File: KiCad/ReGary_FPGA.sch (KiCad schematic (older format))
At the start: 28 parts, among them J1 Conn_01x02, U1 GW1N-UV1P5LQ100, U2 LM1117-3.3, U3 TPS73643DBV

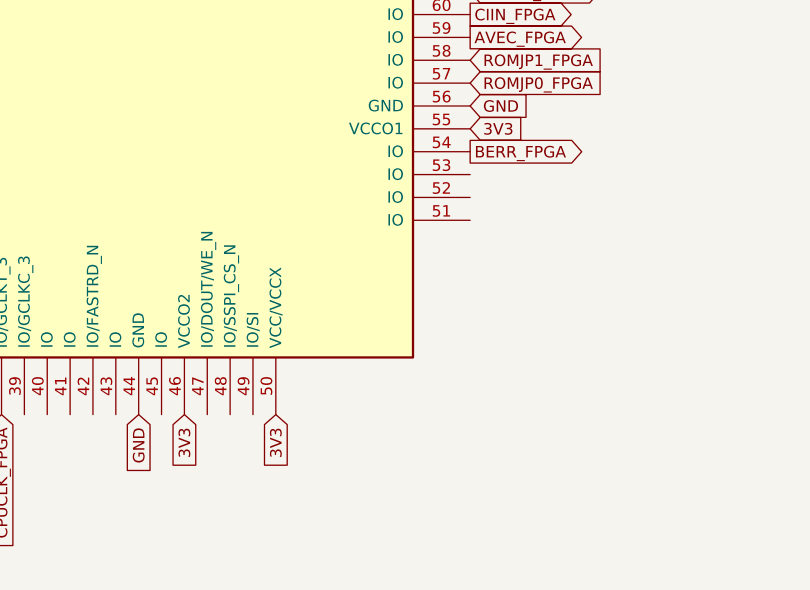
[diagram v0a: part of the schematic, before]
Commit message: More pin assignments and routing
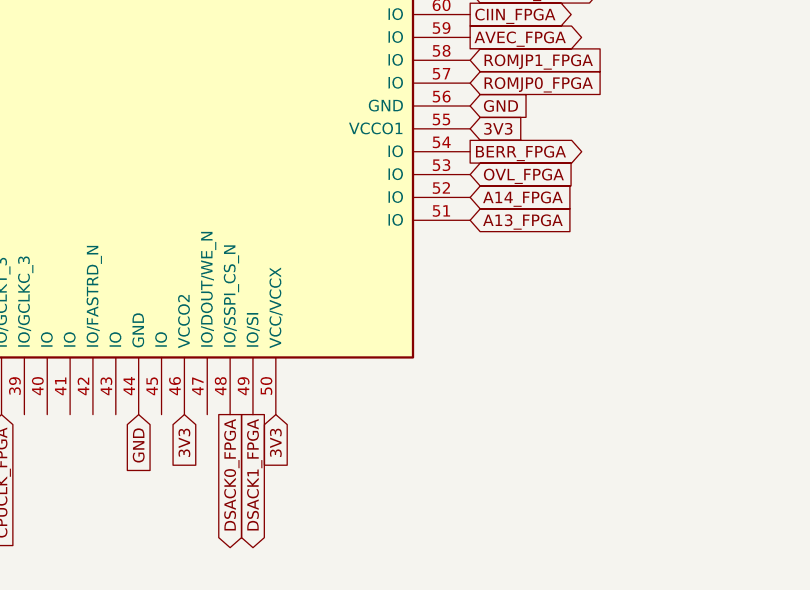
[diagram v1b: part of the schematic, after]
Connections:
- net labels added: A13_FPGA, A14_FPGA, DSACK0_FPGA, DSACK1_FPGA, OVL_FPGA
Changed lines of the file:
@@
 	8650 5150 9000 5150
 Connection ~ 8650 5150
+Text GLabel 5450 5250 2    50   Input ~ 0
+A14_FPGA
+Text GLabel 5450 5150 2    50   Input ~ 0
+OVL_FPGA
+Text GLabel 5450 5350 2    50   Input ~ 0
+A13_FPGA
+Text GLabel 4500 6200 3    50   Output ~ 0
+DSACK1_FPGA
+Text GLabel 4400 6200 3    50   Output ~ 0
+DSACK0_FPGA
 $EndSCHEMATC

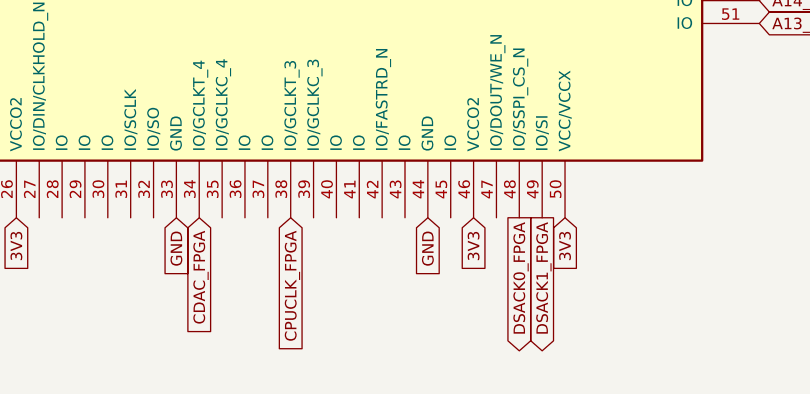
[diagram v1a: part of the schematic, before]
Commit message: More pin assignments and routing
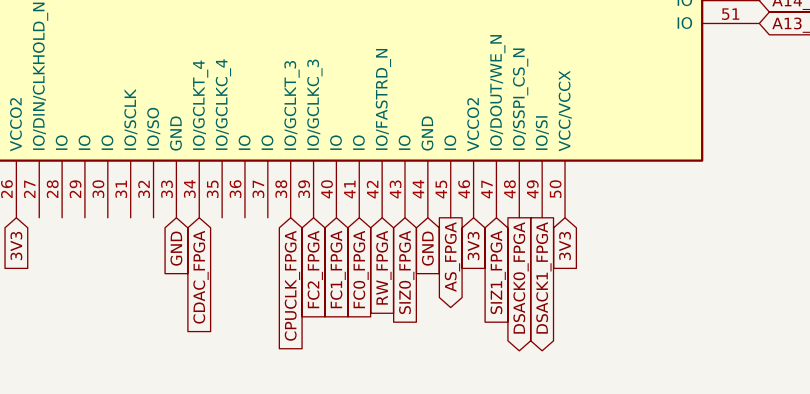
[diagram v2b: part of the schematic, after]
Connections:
- net labels added: AS_FPGA, FC0_FPGA, FC1_FPGA, FC2_FPGA, RW_FPGA, SIZ0_FPGA, SIZ1_FPGA
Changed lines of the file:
@@
 Text GLabel 4400 6200 3    50   Output ~ 0
 DSACK0_FPGA
+Text GLabel 4300 6200 3    50   Input ~ 0
+SIZ1_FPGA
+Text GLabel 3900 6200 3    50   Input ~ 0
+SIZ0_FPGA
+Text GLabel 3800 6200 3    50   Input ~ 0
+RW_FPGA
+Text GLabel 4100 6200 3    50   Output ~ 0
+AS_FPGA
+Text GLabel 3600 6200 3    50   Input ~ 0
+FC1_FPGA
+Text GLabel 3700 6200 3    50   Input ~ 0
+FC0_FPGA
+Text GLabel 3500 6200 3    50   Input ~ 0
+FC2_FPGA
 $EndSCHEMATC

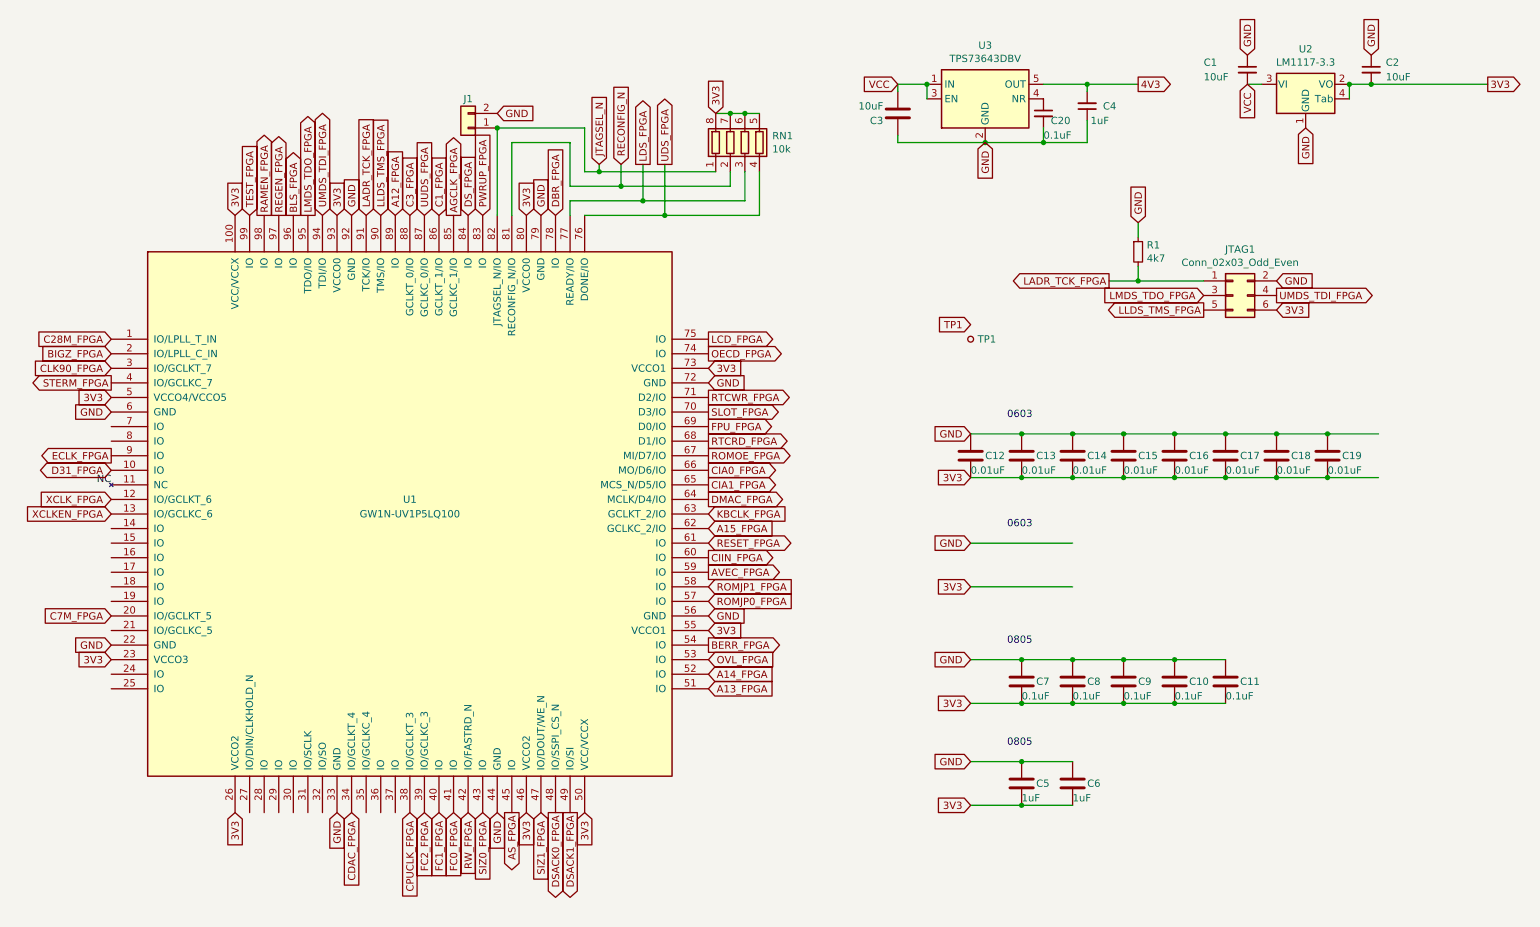
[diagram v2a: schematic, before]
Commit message: More signals to pin assignments and more routing done
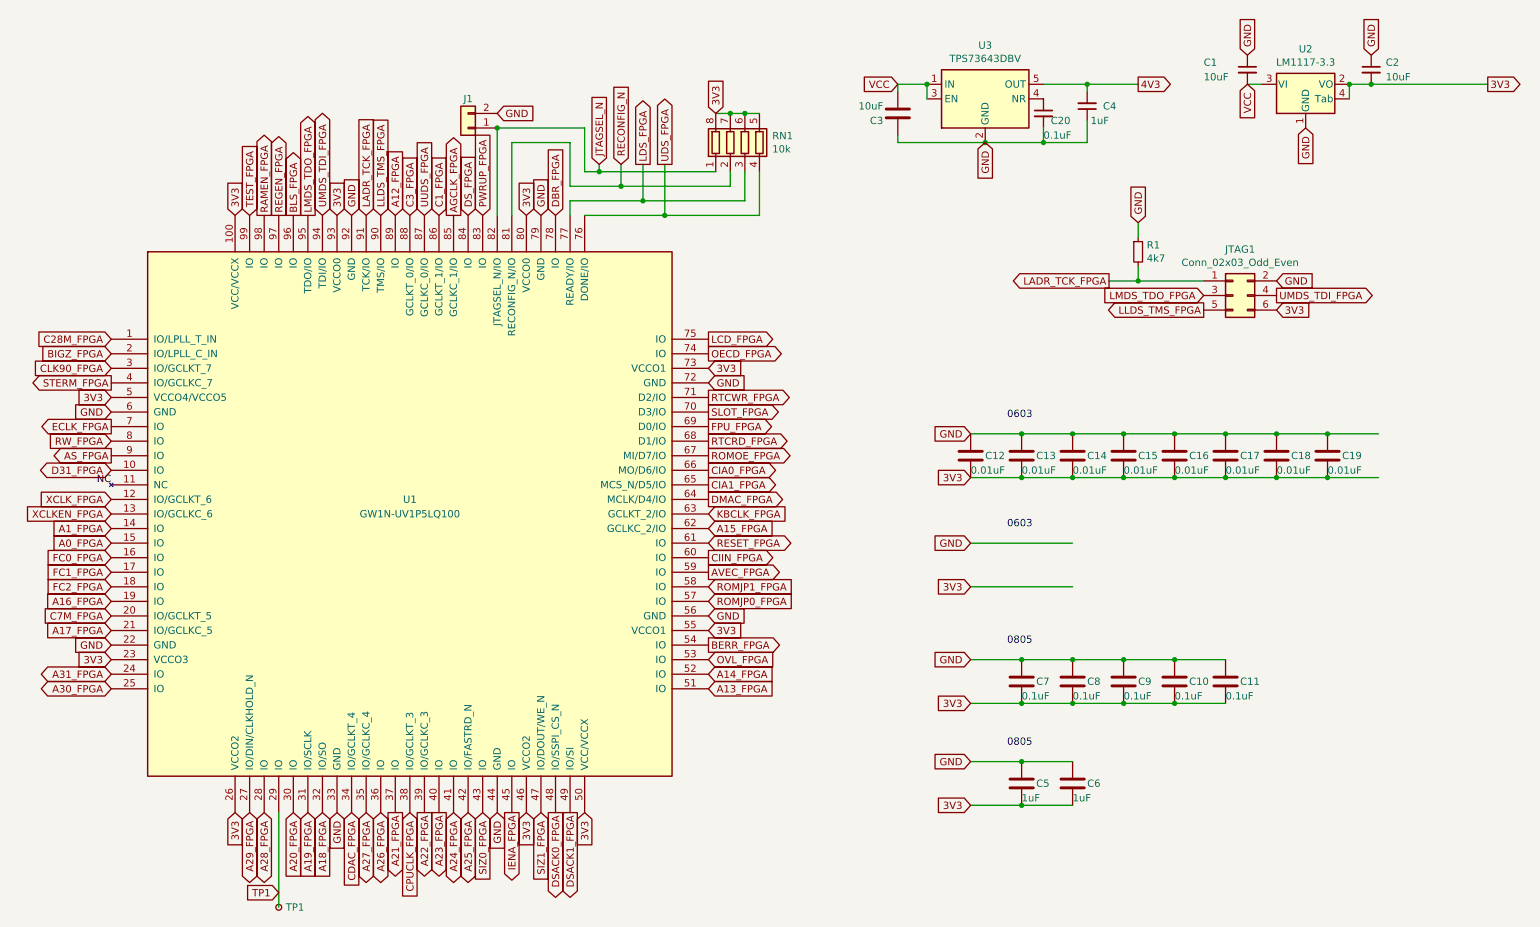
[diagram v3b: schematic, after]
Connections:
- net labels added: A0_FPGA, A16_FPGA, A17_FPGA, A18_FPGA, A19_FPGA, A1_FPGA, A20_FPGA, A21_FPGA, A22_FPGA, A23_FPGA, A24_FPGA, A25_FPGA, A26_FPGA, A27_FPGA, A28_FPGA, A29_FPGA, A30_FPGA, A31_FPGA, IENA_FPGA
- wire segments 77 -> 78
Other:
- moved on the sheet: TP1
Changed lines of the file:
@@
 	-1   0    0    1
 $EndComp
-Text GLabel 7250 2850 0    50   Input ~ 0
+Text GLabel 2500 6750 0    50   Input ~ 0
 TP1
 Wire Wire Line
@@
 L Connector:TestPoint_Small TP1
 U 1 1 655D4DC6
-P 7250 2950
-F 0 "TP1" H 7298 2950 50  0000 L CNN
-F 1 "TestPoint_Small" H 7298 2905 50  0001 L CNN
-F 2 "TestPoint:TestPoint_Pad_1.5x1.5mm" H 7450 2950 50  0001 C CNN
-F 3 "~" H 7450 2950 50  0001 C CNN
-	1    7250 2950
+P 2500 6850
+F 0 "TP1" H 2548 6850 50  0000 L CNN
+F 1 "TestPoint_Small" H 2548 6805 50  0001 L CNN
+F 2 "TestPoint:TestPoint_Pad_1.5x1.5mm" H 2700 6850 50  0001 C CNN
+F 3 "~" H 2700 6850 50  0001 C CNN
+	1    2500 6850
 	1    0    0    -1
 $EndComp
@@
 Text GLabel 3600 2100 1    50   Input ~ 0
 C1_FPGA
-Text GLabel 1350 3750 0    50   Output ~ 0
+Text GLabel 1350 3550 0    50   Output ~ 0
 ECLK_FPGA
 Text GLabel 2400 2100 1    50   Output ~ 0
@@
 Text GLabel 3900 6200 3    50   Input ~ 0
 SIZ0_FPGA
-Text GLabel 3800 6200 3    50   Input ~ 0
+Text GLabel 1350 3650 0    50   Input ~ 0
 RW_FPGA
+Text GLabel 1350 3750 0    50   Output ~ 0
+AS_FPGA
+Text GLabel 1350 4550 0    50   Input ~ 0
+FC1_FPGA
+Text GLabel 1350 4450 0    50   Input ~ 0
+FC0_FPGA
+Text GLabel 1350 4650 0    50   Input ~ 0
+FC2_FPGA
+Text GLabel 1350 4250 0    50   Input ~ 0
+A1_FPGA
+Text GLabel 1350 4350 0    50   Input ~ 0
+A0_FPGA
+Text GLabel 1350 5250 0    50   BiDi ~ 0
+A31_FPGA
+Text GLabel 1350 5350 0    50   BiDi ~ 0
+A30_FPGA
+Text GLabel 2300 6200 3    50   BiDi ~ 0
+A29_FPGA
+Text GLabel 2400 6200 3    50   BiDi ~ 0
+A28_FPGA
+Text GLabel 3100 6200 3    50   BiDi ~ 0
+A27_FPGA
+Text GLabel 3200 6200 3    50   BiDi ~ 0
+A26_FPGA
 Text GLabel 4100 6200 3    50   Output ~ 0
-AS_FPGA
-Text GLabel 3600 6200 3    50   Input ~ 0
-FC1_FPGA
-Text GLabel 3700 6200 3    50   Input ~ 0
-FC0_FPGA
-Text GLabel 3500 6200 3    50   Input ~ 0
-FC2_FPGA
+IENA_FPGA
+Text GLabel 3800 6200 3    50   BiDi ~ 0
+A25_FPGA
+Text GLabel 3700 6200 3    50   BiDi ~ 0
+A24_FPGA
+Text GLabel 1350 4750 0    50   Input ~ 0
+A16_FPGA
+Text GLabel 1350 4950 0    50   Input ~ 0
+A17_FPGA
+Text GLabel 3300 6200 3    50   Output ~ 0
+A21_FPGA
+Text GLabel 3500 6200 3    50   Output ~ 0
+A22_FPGA
+Text GLabel 3600 6200 3    50   Output ~ 0
+A23_FPGA
+Text GLabel 2800 6200 3    50   Input ~ 0
+A18_FPGA
+Text GLabel 2700 6200 3    50   Input ~ 0
+A19_FPGA
+Text GLabel 2600 6200 3    50   Input ~ 0
+A20_FPGA
+Wire Wire Line
+	2500 6200 2500 6850
 $EndSCHEMATC
